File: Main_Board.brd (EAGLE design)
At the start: 128.5 x 95.4 mm, 102 parts, among them J1 SERVO, J5 SPEAKER, J6 SDIO-SDCARD, P1 MOTOR_HEADER, P2 MOTOR_HEADER, P3 JTAG, U1 LMS8117, U10 IMU, U14 TPA2005D1DGN, U2 5V_BUCK_REG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

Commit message: Minor adjustments to spacing
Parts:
- moved R50 1.17 mm to (38.0, 22.7), turned to 90 degrees
- moved C51 1.05 mm to (34.6, 22.8), turned to 90 degrees
- moved C50 0.60 mm to (36.8, 26.4)
- moved AUDIO 0.50 mm to (33.8, 25.5)
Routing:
- net GND: track 513.0 -> 503.7 mm, vias 55 -> 56
- net VCC: track 272.2 -> 265.7 mm
- net BLU_RTS: track 58.6 -> 54.8 mm
- net N$66: track 1.75 -> 3.45 mm
- net N$64: track 1.47 -> 2.92 mm
- net N$65: track 1.45 -> 2.05 mm
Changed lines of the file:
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@@
 <element name="U10" library="BB8" package="IMU_BREAKOUT" value="IMU" x="82.86" y="83.3"/>
 <element name="R44" library="SparkFun-Passives" package="0805" value="150k" x="40.6" y="26.35"/>
-<element name="R50" library="SparkFun-Passives" package="0805" value="150k" x="38.6" y="23.7"/>
+<element name="R50" library="SparkFun-Passives" package="0805" value="150k" x="38" y="22.7" rot="R90"/>
 <element name="C61" library="SparkFun-Capacitors" package="0805" value="1uF" x="41.65" y="16.1" rot="R270"/>
-<element name="C50" library="SparkFun-Capacitors" package="0805" value="1uF" x="37.35" y="26.35"/>
-<element name="C51" library="SparkFun-Capacitors" package="0805" value="1uF" x="35.05" y="23.7" rot="R180"/>
+<element name="C50" library="SparkFun-Capacitors" package="0805" value="1uF" x="36.75" y="26.35"/>
+<element name="C51" library="SparkFun-Capacitors" package="0805" value="1uF" x="34.6" y="22.75" rot="R90"/>
 <element name="U14" library="SparkFun-AnalogIC" package="POWER-SOP8" value="TPA2005D1DGN" x="41.9" y="21.5" rot="R180"/>
 <element name="C9" library="BB8" package="RADIAL_CAN_SMD-G" value="470uF" x="25.8" y="3.8" smashed="yes">
@@
 <element name="R13" library="SparkFun-Passives" package="0805" value="10K" x="91" y="32.4"/>
 <element name="R14" library="SparkFun-Passives" package="0805" value="10k" x="44.2" y="26.2" rot="R270"/>
-<element name="AUDIO" library="testpad" package="B1,27" value="PTR1B1,27" x="34.2" y="25.8" smashed="yes">
-<attribute name="TP_SIGNAL_NAME" value="" x="33.565" y="23.895" size="1" layer="37"/>
-<attribute name="NAME" x="29.765" y="26.616" size="1.27" layer="25" ratio="10"/>
-<attribute name="VALUE" x="33.565" y="25.038" size="0.0254" layer="27"/>
+<element name="AUDIO" library="testpad" package="B1,27" value="PTR1B1,27" x="33.8" y="25.5" smashed="yes">
+<attribute name="TP_SIGNAL_NAME" value="" x="33.165" y="23.595" size="1" layer="37"/>
+<attribute name="NAME" x="29.365" y="26.316" size="1.27" layer="25" ratio="10"/>
+<attribute name="VALUE" x="33.165" y="24.738" size="0.0254" layer="27"/>
 </element>
 <element name="SPEAK" library="testpad" package="B1,27" value="PTR1B1,27" x="36" y="17.6" smashed="yes">
@@
 <wire x1="115.08" y1="51.9" x2="110.94" y2="47.76" width="0.8128" layer="1"/>
 <wire x1="110.94" y1="47.76" x2="108.08" y2="47.76" width="0.8128" layer="1"/>
-<wire x1="62.69" y1="34.19" x2="62.7" y2="34.2" width="2.54" layer="1"/>
-<wire x1="62.7" y1="34.2" x2="62.6" y2="34.2" width="1" layer="1"/>
-<wire x1="62.6" y1="34.2" x2="62.3" y2="34.5" width="1.4224" layer="1"/>
-<wire x1="62.3" y1="34.5" x2="61.2" y2="35.6" width="1.4224" layer="1"/>
-<wire x1="61.2" y1="35.6" x2="33.3" y2="35.6" width="1.4224" layer="1"/>
 <wire x1="33.3" y1="35.6" x2="33.05" y2="35.85" width="1" layer="1"/>
 <via x="23.6" y="45.3" extent="1-16" drill="1"/>
@@
 <wire x1="37.5" y1="37.3" x2="37" y2="36.8" width="0.3048" layer="1"/>
 <wire x1="37" y1="36.8" x2="34" y2="36.8" width="0.3048" layer="1"/>
-<wire x1="34" y1="36.8" x2="33.05" y2="35.85" width="0.3048" layer="1"/>
+<wire x1="34" y1="36.8" x2="33.4" y2="36.2" width="0.3048" layer="1"/>
 <contactref element="F3" pad="2"/>
-<wire x1="54.4" y1="31.4" x2="57.5" y2="34.5" width="2.54" layer="1"/>
-<wire x1="57.5" y1="34.5" x2="62.3" y2="34.5" width="2.54" layer="1"/>
+<wire x1="33.4" y1="36.2" x2="33.05" y2="35.85" width="0.3048" layer="1"/>
 <wire x1="86.1" y1="45.5" x2="86.1" y2="33.2" width="1" layer="1"/>
 <wire x1="86.1" y1="33.2" x2="85.5" y2="32.6" width="1" layer="1"/>
 <wire x1="85.5" y1="32.6" x2="70.7" y2="32.6" width="1" layer="1"/>
 <wire x1="70.7" y1="32.6" x2="69.1" y2="34.2" width="1" layer="1"/>
-<wire x1="69.1" y1="34.2" x2="62.7" y2="34.2" width="1" layer="1"/>
 <wire x1="86.1" y1="45.5" x2="98.45" y2="57.85" width="1" layer="1"/>
 <wire x1="98.45" y1="57.85" x2="99.73" y2="57.85" width="1" layer="1"/>
@@
 <wire x1="104.2" y1="58.1" x2="103.95" y2="57.85" width="1" layer="1"/>
 <wire x1="103.95" y1="57.85" x2="99.73" y2="57.85" width="1" layer="1"/>
+<wire x1="69.1" y1="34.2" x2="57.2" y2="34.2" width="1" layer="1"/>
+<wire x1="57.2" y1="34.2" x2="54.4" y2="31.4" width="1" layer="1"/>
+<wire x1="54.4" y1="31.4" x2="54.4" y2="31.8" width="1.5" layer="1"/>
+<wire x1="54.4" y1="31.8" x2="50.3" y2="35.9" width="1.5" layer="1"/>
+<wire x1="50.3" y1="35.9" x2="33.7" y2="35.9" width="1.5" layer="1"/>
+<wire x1="33.7" y1="35.9" x2="33.4" y2="36.2" width="1.5" layer="1"/>
 </signal>
 <signal name="N$1">
@@
 <wire x1="62.7" y1="59" x2="62.4" y2="59.3" width="0.3048" layer="1"/>
 <wire x1="62.4" y1="59.3" x2="62.4" y2="61.7" width="0.3048" layer="1"/>
-<wire x1="63.1" y1="62.4" x2="64.2" y2="62.4" width="0.3048" layer="1"/>
-<wire x1="64.2" y1="62.4" x2="64.8" y2="63" width="0.3048" layer="1"/>
-<wire x1="64.8" y1="63" x2="64.8" y2="63.5" width="0.3048" layer="1"/>
-<wire x1="64.8" y1="63.5" x2="64.2" y2="64.1" width="0.3048" layer="1"/>
-<wire x1="64.2" y1="64.1" x2="62.4" y2="64.1" width="0.3048" layer="1"/>
 <via x="62.4" y="64.1" extent="1-16" drill="0.34"/>
 <wire x1="62.4" y1="64.1" x2="59.6" y2="67.1" width="0.3048" layer="16"/>
@@
 <wire x1="43.1" y1="76.5" x2="43.1" y2="74.8" width="0.3" layer="1"/>
 <wire x1="43.1" y1="74.8" x2="43.9" y2="74" width="0.3" layer="1"/>
-<wire x1="63.1" y1="62.4" x2="62.9" y2="62.4" width="0.3" layer="1"/>
-<wire x1="62.9" y1="62.4" x2="62.4" y2="61.9" width="0.3" layer="1"/>
-<wire x1="62.4" y1="61.9" x2="62.4" y2="61.7" width="0.3" layer="1"/>
 <wire x1="35.45" y1="84.15" x2="34.8" y2="84.8" width="0.254" layer="1"/>
 <wire x1="34.8" y1="84.8" x2="26.9" y2="84.8" width="0.254" layer="1"/>
 <wire x1="26.9" y1="84.8" x2="26.25" y2="84.15" width="0.254" layer="1"/>
 <wire x1="26.25" y1="84.15" x2="23.7" y2="84.15" width="0.254" layer="1"/>
+<wire x1="62.4" y1="61.7" x2="62.4" y2="64.1" width="0.3" layer="1"/>
 </signal>
 <signal name="SERVO_PWM_3.3">
@@
 <contactref element="R50" pad="2"/>
 <contactref element="U14" pad="4"/>
-<wire x1="39.5" y1="23.7" x2="39.6" y2="23.6" width="0.3" layer="1"/>
-<wire x1="39.6" y1="23.6" x2="40.925" y2="23.6" width="0.3" layer="1"/>
+<wire x1="40.925" y1="23.6" x2="38" y2="23.6" width="0.254" layer="1"/>
 </signal>
 <signal name="N$65">
 <contactref element="R44" pad="1"/>
 <contactref element="C50" pad="2"/>
-<wire x1="38.25" y1="26.35" x2="39.7" y2="26.35" width="0.3" layer="1"/>
+<wire x1="37.65" y1="26.35" x2="39.7" y2="26.35" width="0.3" layer="1"/>
 </signal>
 <signal name="N$66">
 <contactref element="R50" pad="1"/>
 <contactref element="C51" pad="1"/>
-<wire x1="35.95" y1="23.7" x2="37.7" y2="23.7" width="0.3" layer="1"/>
+<wire x1="38" y1="21.8" x2="34.6" y2="21.8" width="0.254" layer="1"/>
+<wire x1="34.6" y1="21.8" x2="34.6" y2="21.85" width="0.254" layer="1"/>
 </signal>
 <signal name="N$67">
@@
 <via x="55.5" y="40.85" extent="1-16" drill="0.34"/>
 <via x="61.4" y="56.45" extent="1-16" drill="0.34"/>
-<wire x1="34.15" y1="23.7" x2="34.2" y2="23.65" width="0.3" layer="1"/>
-<wire x1="34.2" y1="23.65" x2="34.2" y2="22.5" width="0.3" layer="1"/>
-<wire x1="34.2" y1="22.5" x2="35.2" y2="21.5" width="0.3" layer="1"/>
-<wire x1="35.2" y1="21.5" x2="41.9" y2="21.5" width="0.3" layer="1"/>
 <wire x1="63.2" y1="42.15" x2="63.2" y2="42.1" width="0.254" layer="1"/>
 <wire x1="66" y1="40.7" x2="76" y2="40.7" width="0.254" layer="1"/>
@@
 <wire x1="54.7" y1="43" x2="54.6" y2="43" width="0.3" layer="1"/>
 <wire x1="54.6" y1="43" x2="53.2" y2="44.4" width="0.3" layer="1"/>
+<via x="34.5" y="28.5" extent="1-16" drill="0.34"/>
 </signal>
 <signal name="N$136">
@@
 <wire x1="37.8" y1="27.7" x2="37.1" y2="27.7" width="0.2" layer="1"/>
 <wire x1="37.1" y1="27.7" x2="36.45" y2="27.05" width="0.2" layer="1"/>
-<wire x1="36.45" y1="27.05" x2="36.45" y2="26.35" width="0.2" layer="1"/>
+<wire x1="36.45" y1="27.05" x2="35.85" y2="26.35" width="0.2" layer="1"/>
 <contactref element="AUDIO" pad="TP"/>
-<wire x1="36.45" y1="26.35" x2="34.75" y2="26.35" width="0.254" layer="1"/>
-<wire x1="34.75" y1="26.35" x2="34.2" y2="25.8" width="0.254" layer="1"/>
+<wire x1="35.85" y1="26.35" x2="34.75" y2="26.35" width="0.254" layer="1"/>
+<wire x1="34.75" y1="26.35" x2="33.8" y2="25.5" width="0.254" layer="1"/>
 </signal>
 <signal name="N$129">

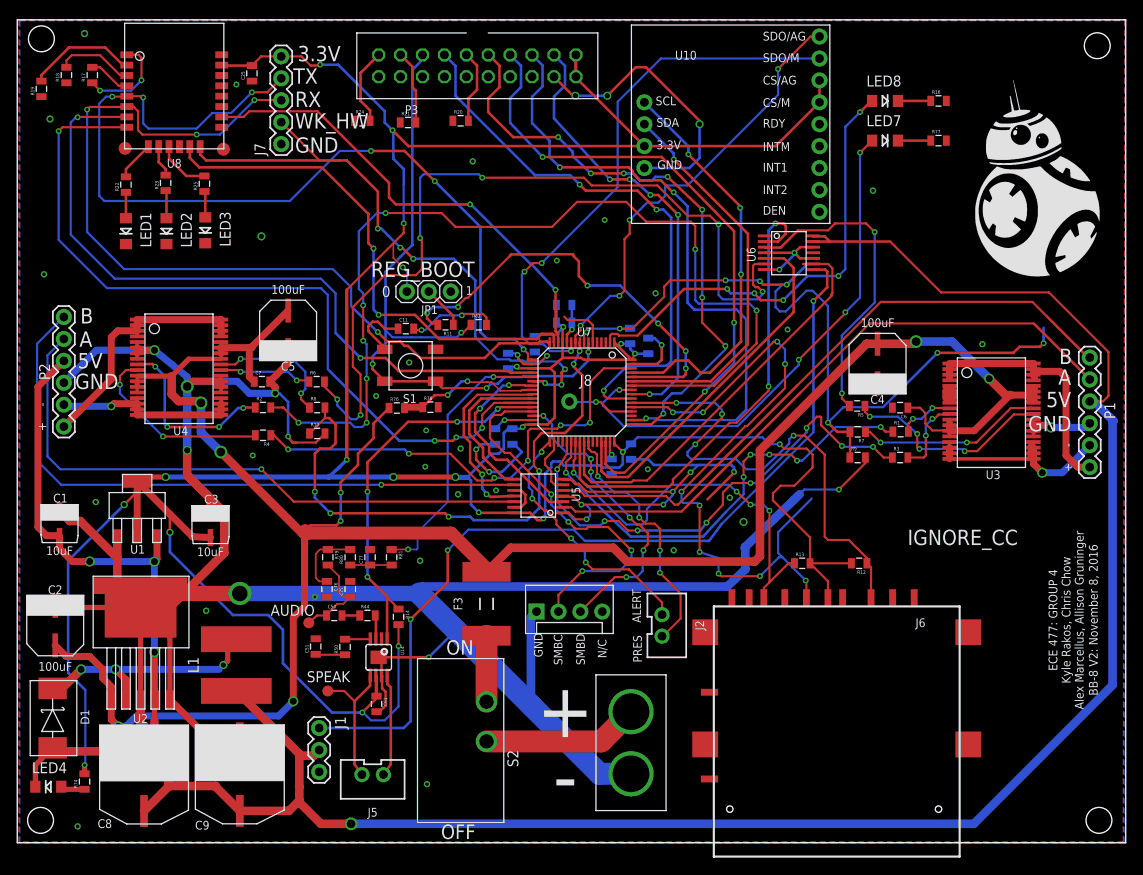
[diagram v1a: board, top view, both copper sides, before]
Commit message: moved some stuff around, kyle please check the board for any final adjustments
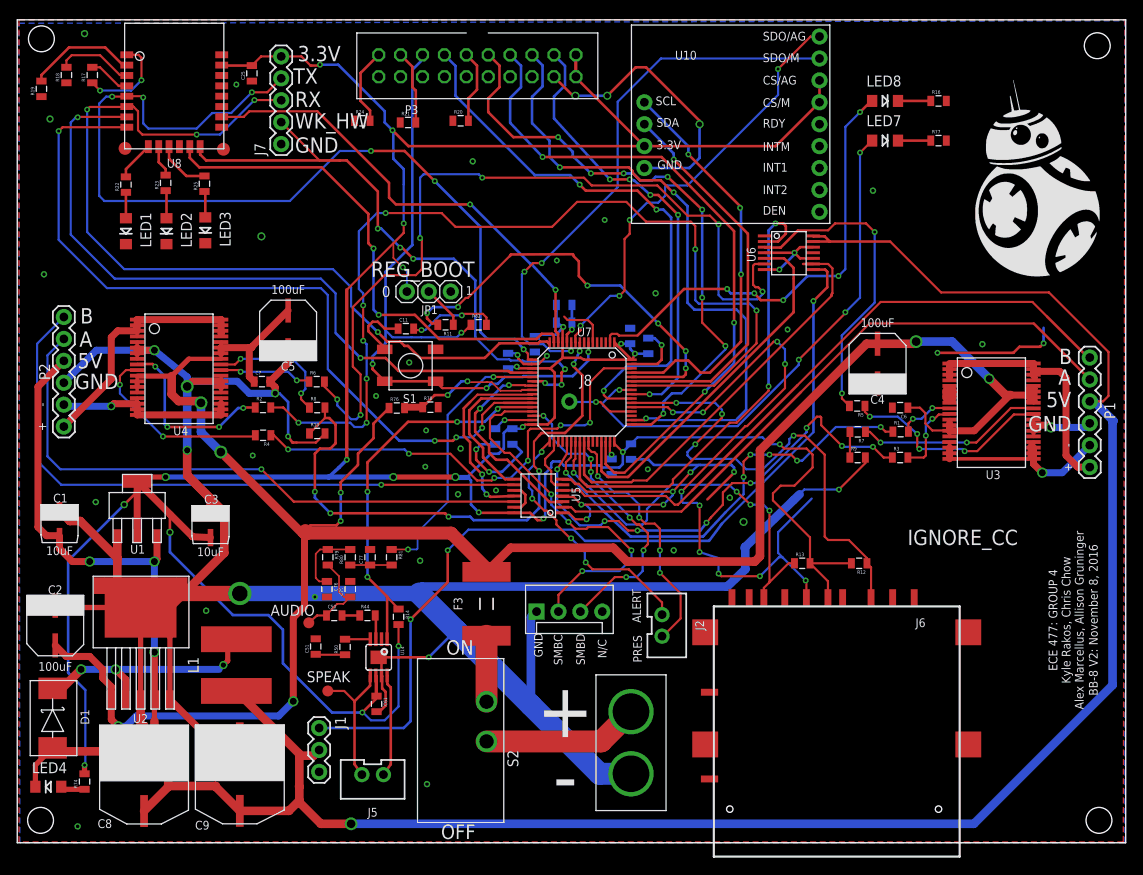
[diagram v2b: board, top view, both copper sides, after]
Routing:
- net MC1_IS: track 92.5 -> 17.5 mm, vias 8 -> 2
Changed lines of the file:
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@@
 <layer number="35" name="tGlue" color="7" fill="4" visible="no" active="yes"/>
 <layer number="36" name="bGlue" color="7" fill="5" visible="no" active="yes"/>
-<layer number="37" name="tTest" color="7" fill="1" visible="no" active="yes"/>
-<layer number="38" name="bTest" color="7" fill="1" visible="no" active="yes"/>
+<layer number="37" name="tTest" color="7" fill="1" visible="yes" active="yes"/>
+<layer number="38" name="bTest" color="7" fill="1" visible="yes" active="yes"/>
 <layer number="39" name="tKeepout" color="4" fill="11" visible="yes" active="yes"/>
 <layer number="40" name="bKeepout" color="1" fill="11" visible="yes" active="yes"/>
@@
 <layer number="42" name="bRestrict" color="1" fill="10" visible="yes" active="yes"/>
 <layer number="43" name="vRestrict" color="2" fill="10" visible="yes" active="yes"/>
-<layer number="44" name="Drills" color="7" fill="1" visible="no" active="yes"/>
+<layer number="44" name="Drills" color="7" fill="1" visible="yes" active="yes"/>
 <layer number="45" name="Holes" color="7" fill="1" visible="yes" active="yes"/>
 <layer number="46" name="Milling" color="3" fill="1" visible="yes" active="yes"/>
@@
 <vertex x="122.7" y="0.7"/>
 </polygon>
-<rectangle x1="102.4" y1="71.2" x2="105.8" y2="74.7" layer="29"/>
-<rectangle x1="132.9" y1="71.3" x2="136.4" y2="74.7" layer="29"/>
-<rectangle x1="133" y1="84.3" x2="136.4" y2="87.7" layer="29"/>
+<rectangle x1="78" y1="9.7" x2="81.4" y2="13.2" layer="29"/>
+<rectangle x1="108.5" y1="9.7" x2="112" y2="13.1" layer="29"/>
+<rectangle x1="108.5" y1="22.6" x2="111.9" y2="26" layer="29"/>
 <rectangle x1="11.4" y1="92.3" x2="25" y2="95.3" layer="41"/>
 <rectangle x1="11.4" y1="92.3" x2="25.1" y2="95.4" layer="42"/>
@@
 <text x="124.7455625" y="25.828803125" size="1.016" layer="21" font="vector" rot="R270" align="center">BB-8 V2: November 8, 2016</text>
 <rectangle x1="84" y1="17.4" x2="104.8" y2="21.4" layer="41"/>
-<rectangle x1="102.6" y1="84.4" x2="105.7" y2="87.6" layer="29"/>
+<rectangle x1="78.2" y1="22.8" x2="81.3" y2="26" layer="29"/>
 <rectangle x1="117.911346875" y1="65.649578125" x2="118.546346875" y2="65.674978125" layer="21"/>
 <rectangle x1="117.504946875" y1="65.674978125" x2="118.952746875" y2="65.700378125" layer="21"/>
@@
 <wire x1="115.48" y1="56.8" x2="106.68" y2="56.8" width="0.3048" layer="1"/>
 <via x="106.68" y="56.8" extent="1-16" drill="0.34"/>
-<wire x1="106.68" y1="56.8" x2="101.68" y2="51.8" width="0.3048" layer="16"/>
-<via x="93.98" y="48.7" extent="1-16" drill="0.34"/>
-<wire x1="93.98" y1="48.7" x2="95.04" y2="47.64" width="0.3048" layer="1"/>
-<wire x1="95.04" y1="47.64" x2="96.53" y2="47.64" width="0.3048" layer="1"/>
 <wire x1="118.98" y1="58.7" x2="118.98" y2="59.7" width="0.3" layer="16"/>
-<wire x1="91.3" y1="66.8" x2="89.2" y2="64.7" width="0.3" layer="16"/>
-<via x="89.2" y="64.7" extent="1-16" drill="0.34"/>
-<wire x1="89.2" y1="64.7" x2="86.5" y2="64.7" width="0.3" layer="1"/>
-<wire x1="86.5" y1="64.7" x2="86.1" y2="65.1" width="0.3" layer="1"/>
-<via x="86.1" y="65.1" extent="1-16" drill="0.34"/>
-<via x="82.1" y="65.2" extent="1-16" drill="0.34"/>
-<wire x1="71.3" y1="59.6" x2="69.85" y2="59.6" width="0.3" layer="1"/>
-<via x="69.85" y="59.6" extent="1-16" drill="0.34"/>
-<wire x1="65.72" y1="58" x2="65.7" y2="58.02" width="0.254" layer="1"/>
-<wire x1="65.7" y1="58.02" x2="65.7" y2="58.9" width="0.254" layer="1"/>
-<via x="66" y="59.2" extent="1-16" drill="0.34"/>
-<wire x1="66.4" y1="59.6" x2="69.85" y2="59.6" width="0.254" layer="16"/>
-<wire x1="71.3" y1="59.6" x2="75" y2="63.3" width="0.254" layer="1"/>
-<wire x1="75" y1="63.3" x2="75" y2="64.5" width="0.254" layer="1"/>
-<wire x1="75.7" y1="65.2" x2="75" y2="64.5" width="0.254" layer="1"/>
-<wire x1="82.1" y1="65.2" x2="86" y2="65.2" width="0.254" layer="16"/>
-<wire x1="86" y1="65.2" x2="86.1" y2="65.1" width="0.254" layer="16"/>
-<wire x1="82.1" y1="65.2" x2="75.7" y2="65.2" width="0.254" layer="1"/>
-<wire x1="93.98" y1="48.7" x2="93.98" y2="62.22" width="0.254" layer="16"/>
-<wire x1="93.98" y1="62.22" x2="92.2" y2="64" width="0.254" layer="16"/>
-<wire x1="92.2" y1="64" x2="91.5" y2="64" width="0.254" layer="16"/>
-<wire x1="91.5" y1="64" x2="89.1" y2="61.6" width="0.254" layer="16"/>
-<wire x1="89.1" y1="61.6" x2="88.4" y2="61.6" width="0.254" layer="16"/>
-<wire x1="88.4" y1="61.6" x2="87.9" y2="62.1" width="0.254" layer="16"/>
-<wire x1="87.9" y1="62.1" x2="87.9" y2="63.9" width="0.254" layer="16"/>
-<wire x1="87.9" y1="63.9" x2="88.7" y2="64.7" width="0.254" layer="16"/>
-<wire x1="88.7" y1="64.7" x2="89.2" y2="64.7" width="0.254" layer="16"/>
-<wire x1="101.68" y1="51.8" x2="100.38" y2="50.5" width="0.254" layer="16"/>
-<wire x1="100.38" y1="50.5" x2="95.78" y2="50.5" width="0.254" layer="16"/>
-<wire x1="95.78" y1="50.5" x2="93.98" y2="48.7" width="0.254" layer="16"/>
-<wire x1="66.4" y1="59.6" x2="66" y2="59.2" width="0.254" layer="16"/>
-<wire x1="65.7" y1="58.9" x2="66" y2="59.2" width="0.254" layer="1"/>
+<wire x1="96.53" y1="47.64" x2="106.68" y2="56.8" width="0" layer="19" extent="1-1"/>
+<wire x1="65.72" y1="58" x2="96.53" y2="47.64" width="0" layer="19" extent="1-1"/>
 </signal>
 <signal name="N$5">
@@
 <vertex x="128.4" y="0"/>
 <vertex x="0.3" y="0"/>
-<vertex x="0.3" y="95.3"/>
+<vertex x="0.2" y="95"/>
 <vertex x="128.4" y="95.3"/>
 </polygon>

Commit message: Made board smaller, finished routing, added new test via, ect.
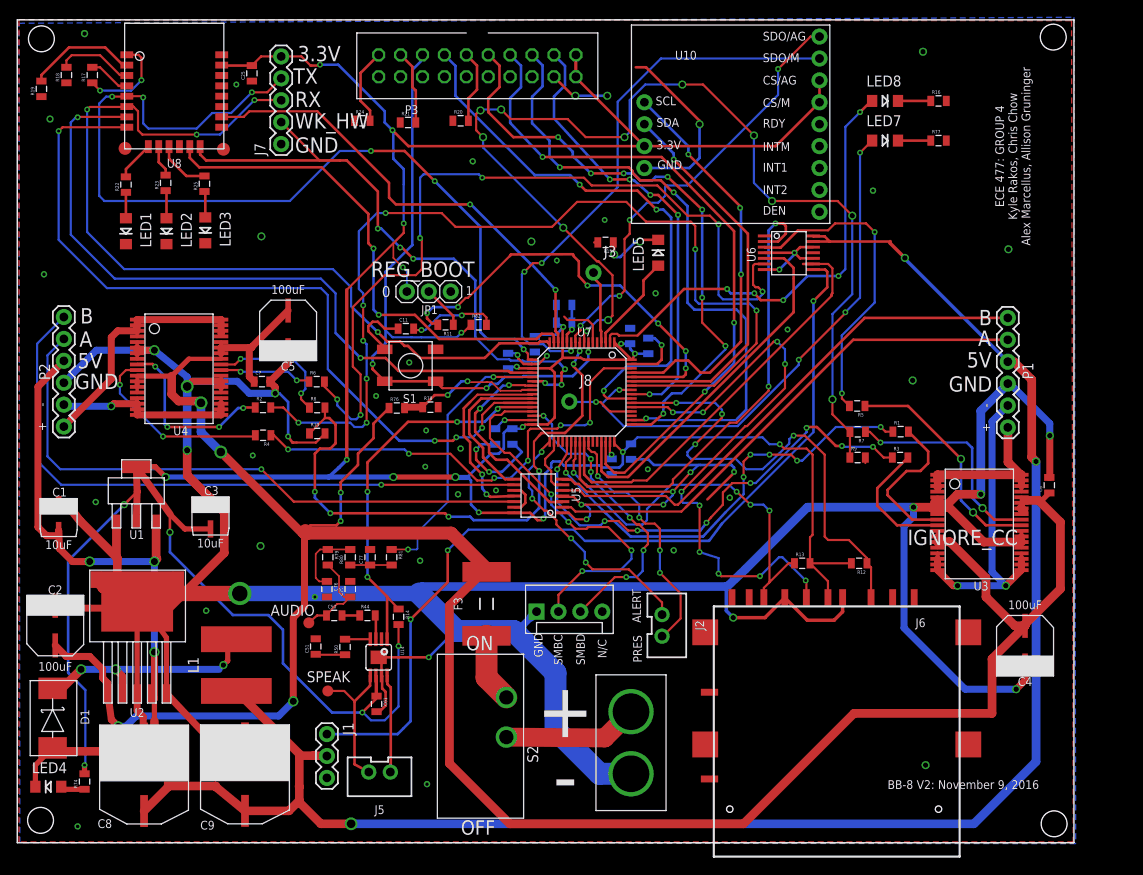
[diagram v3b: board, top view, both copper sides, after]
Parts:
- added J3: (no value), SparkFun-Connectors:1X01_NO_SILK
- added LED5: (no value), LilyPad-Wearables:LED-1206
- added R15: 100, SparkFun-Resistors:0805
- moved C4 36.9 mm to (116.8, 25.1)
- moved C6 19.5 mm to (119.6, 41.5), turned to 90 degrees
- moved U3 13.0 mm to (106.7, 31.6)
- moved P1 10.6 mm to (114.8, 54.5)
- moved S2 2.35 mm to (56.7, 16.9)
- moved U1 1.70 mm to (13.8, 37.3)
- moved J1 1.14 mm to (35.9, 12.6)
- moved C3 1.00 mm to (22.4, 36.5)
- moved J5 0.85 mm to (42.0, 7.65)
- moved U2 0.81 mm to (10.5, 17.3)
- moved C1 0.71 mm to (4.80, 36.3)
- moved C9 0.60 mm to (26.4, 3.80)
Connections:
- removed net N$21: U7.P$4
- new net N$12: LED5.C, R15.1
- new net N$17: J3.1, U7.P$4
- net GND: now also R15.2
- net N$29: now also LED5.A
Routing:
- net MC1_IS: track 17.5 -> 124.4 mm, vias 2 -> 12
- net GND: track 503.7 -> 593.6 mm, vias 56 -> 62
- net VCC: track 265.7 -> 304.5 mm, vias 8 -> 6
- net N$2: track 24.1 -> 40.7 mm, vias 1 -> 2
- net M1_A_5: track 73.1 -> 60.1 mm
- net M1_B_5: track 74.3 -> 61.3 mm
- net 5V: track 292.1 -> 279.4 mm, vias 4 -> 6
- net N$1: track 32.1 -> 19.8 mm
- net N$3: track 6.49 -> 18.1 mm, vias 2 -> 0
- net N$29: track 0.00 -> 11.4 mm
- net SDIO_CK: track 79.2 -> 70.6 mm
- net N$17: track 0.00 -> 8.48 mm
- net N$12: track 0.00 -> 7.49 mm, vias 0 -> 2
- net N$4: track 8.97 -> 15.0 mm, vias 2 -> 0
- net N$5: track 21.7 -> 25.7 mm
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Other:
- board size 128.5 x 95.4 mm -> 122.5 x 95.4 mm
- board text added: "BB-8 V2: November 9, 2016"
- board text removed: "BB-8 V2: November 8, 2016"
